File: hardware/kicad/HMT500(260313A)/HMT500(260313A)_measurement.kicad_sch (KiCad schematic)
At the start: 15 parts, among them J3 SM04B-SRSS-TB, U5 PCAP04-AQFM-24, U6 ADS1220IPWR

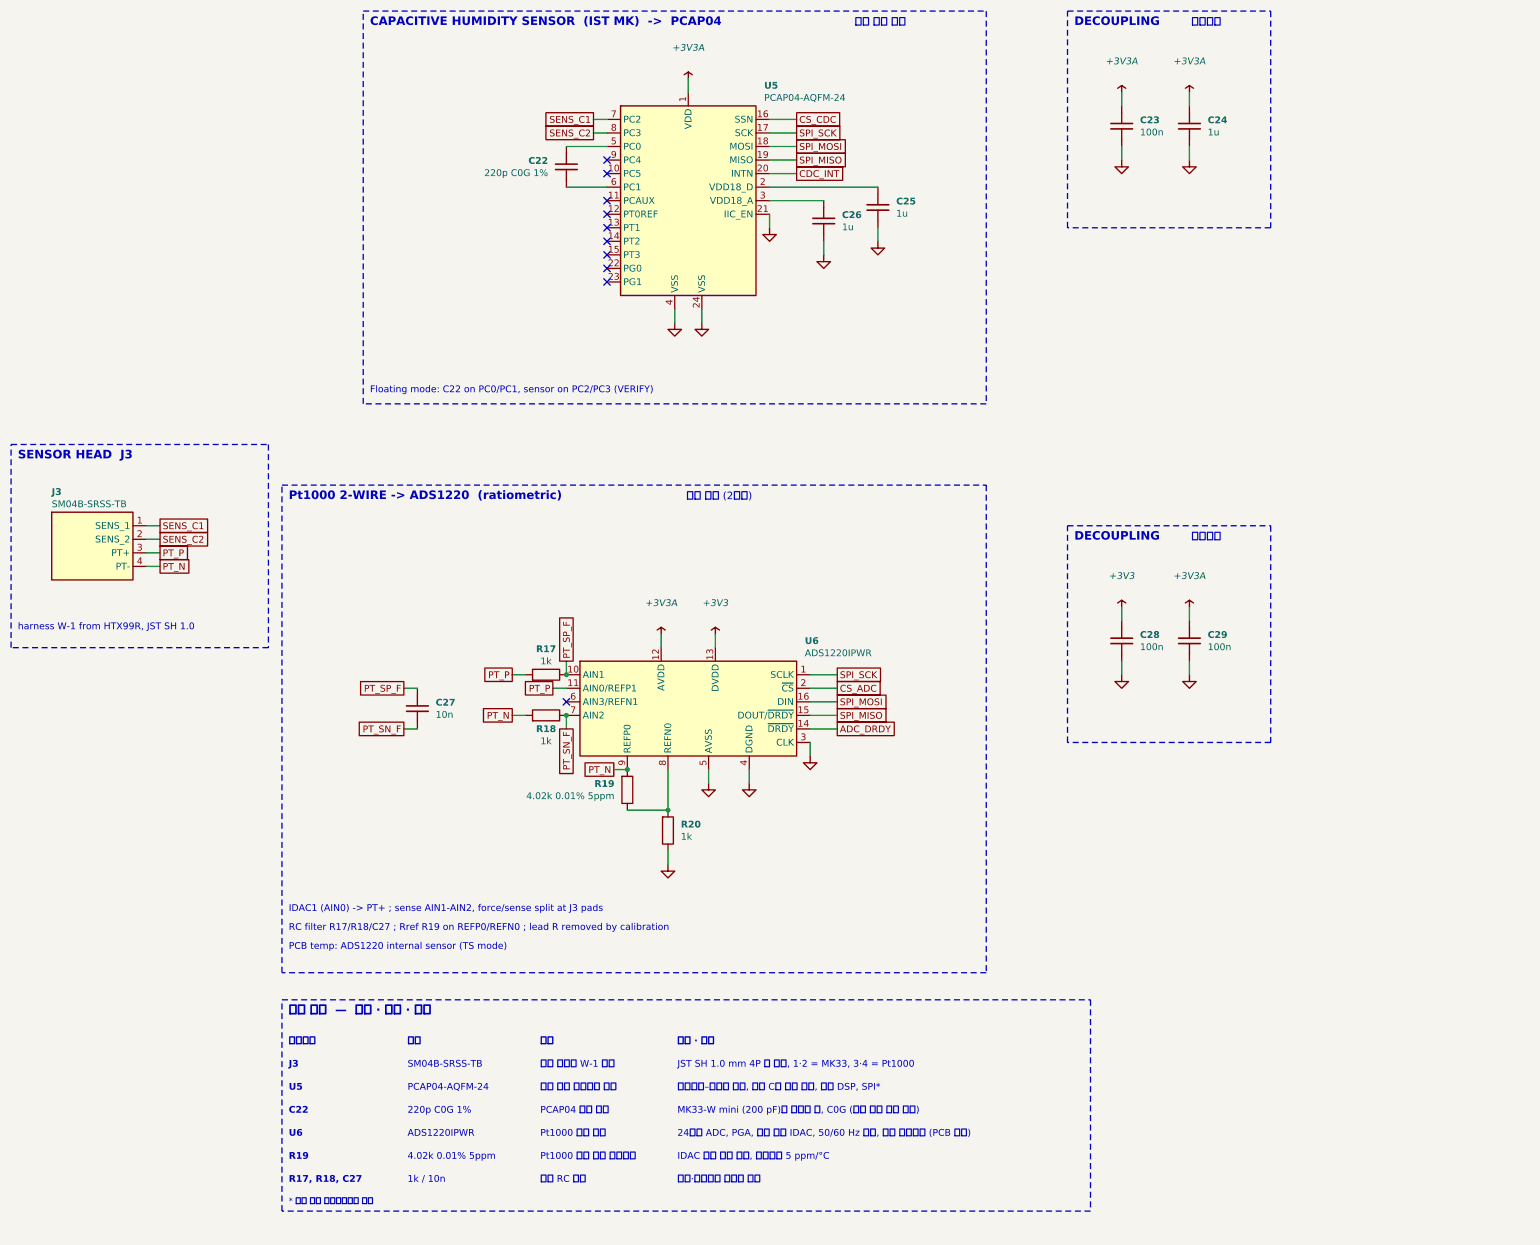
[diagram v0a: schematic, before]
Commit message: Schematic v0.8: apply datasheet review A-O (HMT500(260313A))
- Real pinouts from manufacturer datasheets: LMR36006BRNXR (RNX-12),
  TPS26611DDFR (SOT-23-8), PCAP04 (QFN24); TPS2660 PowerPAD = RTN
- TPS2660: RTN isolated from GND (R22, R7 removed); R5/R6/C4/MODE on
  EF_RTN; R6 80.6k (149 mA); R5 41.2k -> OVP 29 V, supply 12-28 V so
  TPS26611 +Vs stays <= 30 V
- DAC SPI: per-DAC SCLK gating (74LVC2G32, SPI2 mode 3, LATCH1/2 on
  PB10/PB11) - daisy chain was removed in DAC8760 rev D
- DAC AVDD 10R series, ALARM wired-OR with 10k pull-up (PB6)
- Output TVS -> TVS3301 (stacked-pin two-terminal symbol)
- PCAP04 on dedicated SPI3 (PB3/4/5), VDD18 4.7uF, VDD33 10uF
- Buck per datasheet: L 15uH, COUT 2x22uF, CFF 20pF
- Shared VIN_P bulk (C53, C26 removed); PWR_FLT PB7; SGOOD -> PC6/PC7
- Parts list, circuit-design, decision log #26, review doc updated;
  netlist 74/74, 0 errors; tests pass

Co-Authored-By: Claude Opus 5.5 <noreply@anthropic.com>
Claude-Session: https://claude.ai/code/session_01JA2o8uJsqp9Vzsg4b665ev
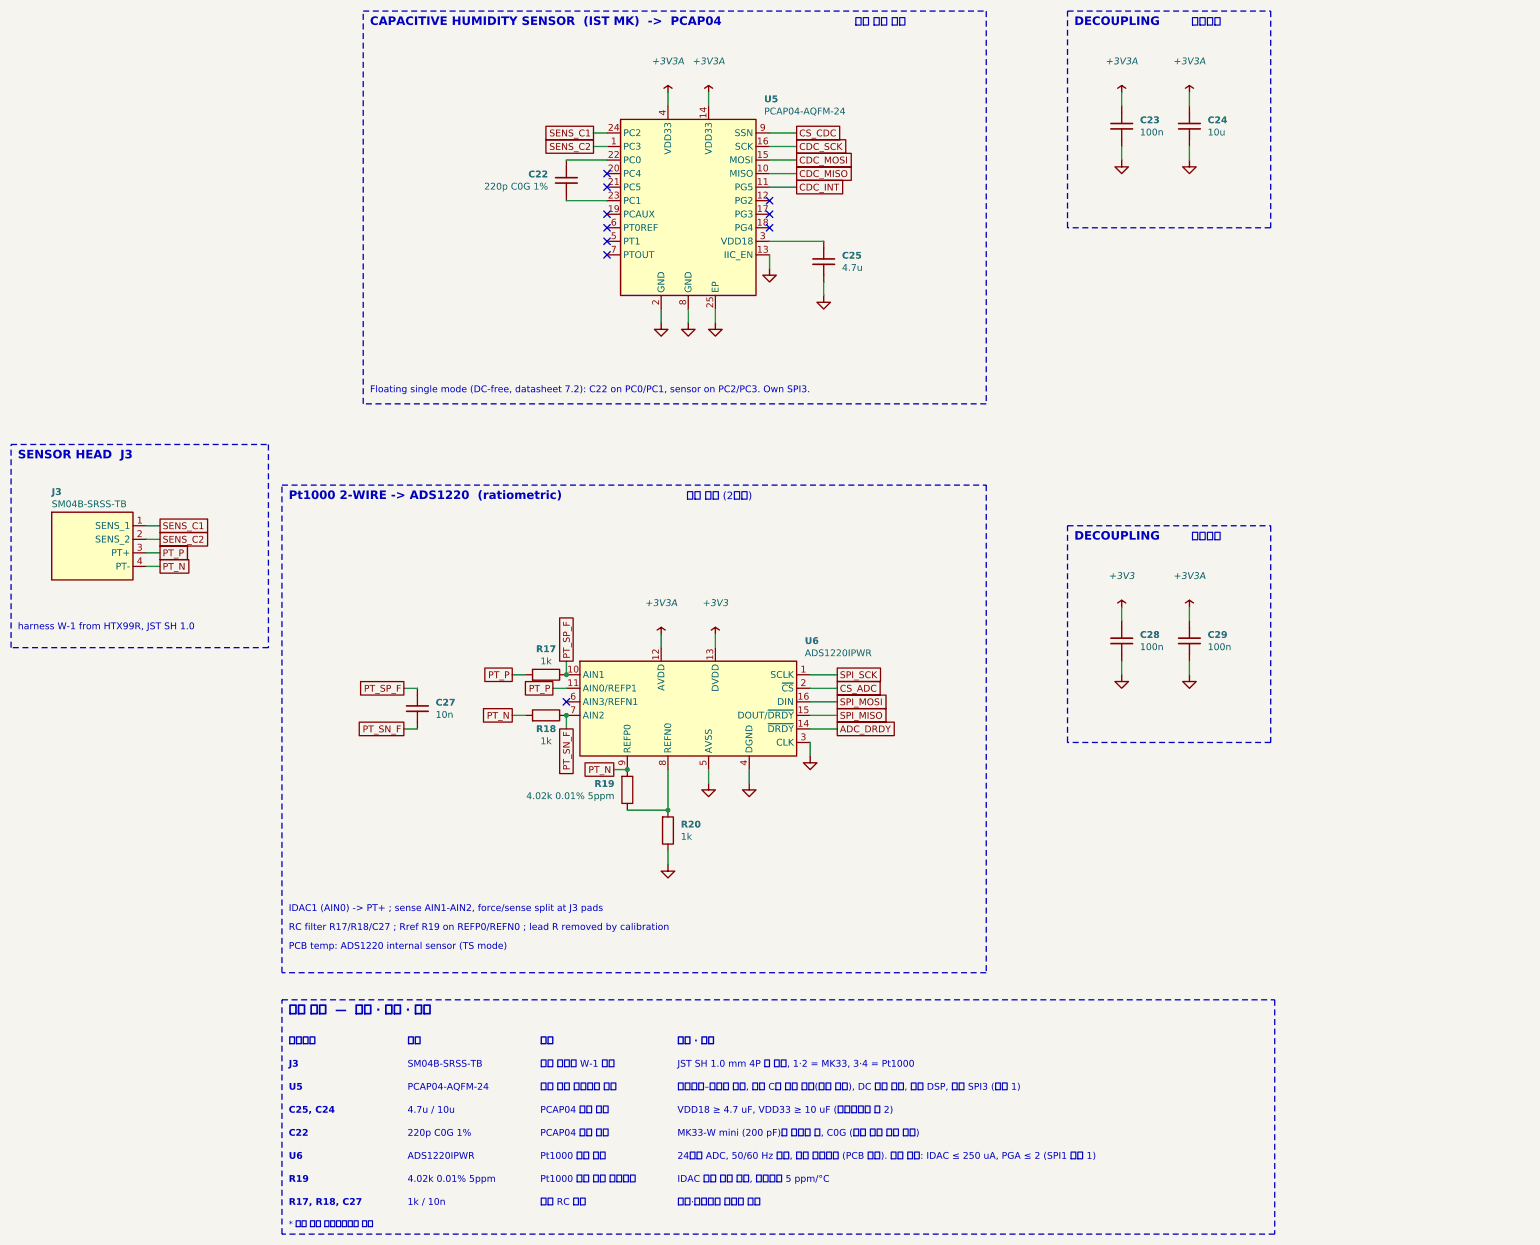
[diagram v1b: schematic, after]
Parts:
- removed C26: 1u, Capacitor_SMD:C_0603_1608Metric, symbol HMT500_260313A:C
- C24: value 1u -> 10u; footprint Capacitor_SMD:C_0603_1608Metric -> Capacitor_SMD:C_0805_2012Metric
- C25: value 1u -> 4.7u; footprint Capacitor_SMD:C_0603_1608Metric -> Capacitor_SMD:C_0805_2012Metric
- U5: footprint TBD:QFN-24_PCAP04 -> Package_DFN_QFN:QFN-24-1EP_4x4mm_P0.5mm_EP2.6x2.6mm; VERIFY YES - pin numbers are placeholders -> (none)
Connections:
- net +3V3A: now also U5.14 (VDD33), U5.4 (VDD33); no longer U5.1 (VDD)
- net CDC_INT: now also U5.11 (PG5); no longer U5.20 (INTN)
- net CS_CDC: now also U5.9 (SSN); no longer U5.16 (SSN)
- net GND: now also U5.13 (IIC_EN), U5.2 (GND), U5.25 (EP), U5.8 (GND); no longer U5.21 (IIC_EN), U5.24 (VSS), U5.4 (VSS)
- net SENS_C1: now also U5.24 (PC2); no longer U5.7 (PC2)
- net SENS_C2: now also U5.1 (PC3); no longer U5.8 (PC3)
- net SPI_MISO: no longer U5.19 (MISO)
- net SPI_MOSI: no longer U5.18 (MOSI)
- net SPI_SCK: no longer U5.17 (SCK)
- net CDC_MISO: now reaches U5.10 (MISO)
- net CDC_MOSI: now reaches U5.15 (MOSI)
- net at C25.1: now also U5.3 (VDD18); no longer U5.2 (VDD18_D)
- net at U5.22 (PC0): now also C22.1
- net at U5.23 (PC1): now also C22.2
- net at U5.5 (PT1): no longer C22.1
- net at U5.6 (PT0REF): no longer C22.2
- new net CDC_SCK: U5.16 (SCK)
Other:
- note added: "24비트 ADC, 50/60 Hz 제거, 내부 온도센서 (PCB 온도). 설정 한계: IDAC ≤ 250 uA, PGA ≤ 2 (SPI1 모드 1)"
- note added: "4.7u / 10u"
- note added: "C25, C24"
- note added: "Floating single mode (DC-free, datasheet 7.2): C22 on PC0/PC1, sensor on PC2/PC3. Own SPI3."
- note added: "PCAP04 전원 버퍼"
- note added: "VDD18 ≥ 4.7 uF, VDD33 ≥ 10 uF (데이터시트 표 2)"
- note added: "정전용량–디지털 변환, 기준 C와 비율 측정(방전 시간), DC 없는 구동, 내부 DSP, 전용 SPI3 (모드 1)"
- note removed: "24비트 ADC, PGA, 여기 전류 IDAC, 50/60 Hz 제거, 내부 온도센서 (PCB 온도)"
- note removed: "Floating mode: C22 on PC0/PC1, sensor on PC2/PC3 (VERIFY)"
- note removed: "정전용량–디지털 변환, 기준 C와 비율 측정, 내부 DSP, SPI*"
- moved on the sheet: C22, C25

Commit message: Schematic: global label shape shows signal direction (driver = output, receiver = input)
Direction derived per net from pin types (output / tri-state / open-drain
drivers, MCU as driver when only inputs are on the other side); analog
and passive nets keep the plain shape, RS-485 bus bidirectional.
Legend line on the root sheet; test for key nets.

Co-Authored-By: Claude Opus 5.5 <noreply@anthropic.com>
Claude-Session: https://claude.ai/code/session_01JA2o8uJsqp9Vzsg4b665ev
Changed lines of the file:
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@@
 (global_label "SENS_C1" (shape passive) (at 124.46 60.96 180) (fields_autoplaced) (effects (font (size 1.27 1.27)) (justify right)) (property "Intersheetrefs" "${INTERSHEET_REFS}" (at 124.46 60.96 0) (effects (font (size 1.27 1.27)) hide)))
 (global_label "SENS_C2" (shape passive) (at 124.46 63.5 180) (fields_autoplaced) (effects (font (size 1.27 1.27)) (justify right)) (property "Intersheetrefs" "${INTERSHEET_REFS}" (at 124.46 63.5 0) (effects (font (size 1.27 1.27)) hide)))
-(global_label "CS_CDC" (shape passive) (at 162.56 60.96 0) (fields_autoplaced) (effects (font (size 1.27 1.27)) (justify left)) (property "Intersheetrefs" "${INTERSHEET_REFS}" (at 162.56 60.96 0) (effects (font (size 1.27 1.27)) hide)))
-(global_label "CDC_SCK" (shape passive) (at 162.56 63.5 0) (fields_autoplaced) (effects (font (size 1.27 1.27)) (justify left)) (property "Intersheetrefs" "${INTERSHEET_REFS}" (at 162.56 63.5 0) (effects (font (size 1.27 1.27)) hide)))
-(global_label "CDC_MOSI" (shape passive) (at 162.56 66.04 0) (fields_autoplaced) (effects (font (size 1.27 1.27)) (justify left)) (property "Intersheetrefs" "${INTERSHEET_REFS}" (at 162.56 66.04 0) (effects (font (size 1.27 1.27)) hide)))
-(global_label "CDC_MISO" (shape passive) (at 162.56 68.58 0) (fields_autoplaced) (effects (font (size 1.27 1.27)) (justify left)) (property "Intersheetrefs" "${INTERSHEET_REFS}" (at 162.56 68.58 0) (effects (font (size 1.27 1.27)) hide)))
-(global_label "CDC_INT" (shape passive) (at 162.56 71.12 0) (fields_autoplaced) (effects (font (size 1.27 1.27)) (justify left)) (property "Intersheetrefs" "${INTERSHEET_REFS}" (at 162.56 71.12 0) (effects (font (size 1.27 1.27)) hide)))
+(global_label "CS_CDC" (shape input) (at 162.56 60.96 0) (fields_autoplaced) (effects (font (size 1.27 1.27)) (justify left)) (property "Intersheetrefs" "${INTERSHEET_REFS}" (at 162.56 60.96 0) (effects (font (size 1.27 1.27)) hide)))
+(global_label "CDC_SCK" (shape input) (at 162.56 63.5 0) (fields_autoplaced) (effects (font (size 1.27 1.27)) (justify left)) (property "Intersheetrefs" "${INTERSHEET_REFS}" (at 162.56 63.5 0) (effects (font (size 1.27 1.27)) hide)))
+(global_label "CDC_MOSI" (shape input) (at 162.56 66.04 0) (fields_autoplaced) (effects (font (size 1.27 1.27)) (justify left)) (property "Intersheetrefs" "${INTERSHEET_REFS}" (at 162.56 66.04 0) (effects (font (size 1.27 1.27)) hide)))
+(global_label "CDC_MISO" (shape output) (at 162.56 68.58 0) (fields_autoplaced) (effects (font (size 1.27 1.27)) (justify left)) (property "Intersheetrefs" "${INTERSHEET_REFS}" (at 162.56 68.58 0) (effects (font (size 1.27 1.27)) hide)))
+(global_label "CDC_INT" (shape output) (at 162.56 71.12 0) (fields_autoplaced) (effects (font (size 1.27 1.27)) (justify left)) (property "Intersheetrefs" "${INTERSHEET_REFS}" (at 162.56 71.12 0) (effects (font (size 1.27 1.27)) hide)))
 (global_label "PT_P" (shape passive) (at 109.22 162.56 180) (fields_autoplaced) (effects (font (size 1.27 1.27)) (justify right)) (property "Intersheetrefs" "${INTERSHEET_REFS}" (at 109.22 162.56 0) (effects (font (size 1.27 1.27)) hide)))
 (global_label "PT_N" (shape passive) (at 109.22 170.18 180) (fields_autoplaced) (effects (font (size 1.27 1.27)) (justify right)) (property "Intersheetrefs" "${INTERSHEET_REFS}" (at 109.22 170.18 0) (effects (font (size 1.27 1.27)) hide)))
@@
 (global_label "PT_SN_F" (shape passive) (at 88.9 172.72 180) (fields_autoplaced) (effects (font (size 1.27 1.27)) (justify right)) (property "Intersheetrefs" "${INTERSHEET_REFS}" (at 88.9 172.72 0) (effects (font (size 1.27 1.27)) hide)))
 (global_label "PT_N" (shape passive) (at 128.27 180.34 180) (fields_autoplaced) (effects (font (size 1.27 1.27)) (justify right)) (property "Intersheetrefs" "${INTERSHEET_REFS}" (at 128.27 180.34 0) (effects (font (size 1.27 1.27)) hide)))
-(global_label "SPI_SCK" (shape passive) (at 170.18 162.56 0) (fields_autoplaced) (effects (font (size 1.27 1.27)) (justify left)) (property "Intersheetrefs" "${INTERSHEET_REFS}" (at 170.18 162.56 0) (effects (font (size 1.27 1.27)) hide)))
-(global_label "CS_ADC" (shape passive) (at 170.18 165.1 0) (fields_autoplaced) (effects (font (size 1.27 1.27)) (justify left)) (property "Intersheetrefs" "${INTERSHEET_REFS}" (at 170.18 165.1 0) (effects (font (size 1.27 1.27)) hide)))
-(global_label "SPI_MOSI" (shape passive) (at 170.18 167.64 0) (fields_autoplaced) (effects (font (size 1.27 1.27)) (justify left)) (property "Intersheetrefs" "${INTERSHEET_REFS}" (at 170.18 167.64 0) (effects (font (size 1.27 1.27)) hide)))
-(global_label "SPI_MISO" (shape passive) (at 170.18 170.18 0) (fields_autoplaced) (effects (font (size 1.27 1.27)) (justify left)) (property "Intersheetrefs" "${INTERSHEET_REFS}" (at 170.18 170.18 0) (effects (font (size 1.27 1.27)) hide)))
-(global_label "ADC_DRDY" (shape passive) (at 170.18 172.72 0) (fields_autoplaced) (effects (font (size 1.27 1.27)) (justify left)) (property "Intersheetrefs" "${INTERSHEET_REFS}" (at 170.18 172.72 0) (effects (font (size 1.27 1.27)) hide)))
+(global_label "SPI_SCK" (shape input) (at 170.18 162.56 0) (fields_autoplaced) (effects (font (size 1.27 1.27)) (justify left)) (property "Intersheetrefs" "${INTERSHEET_REFS}" (at 170.18 162.56 0) (effects (font (size 1.27 1.27)) hide)))
+(global_label "CS_ADC" (shape input) (at 170.18 165.1 0) (fields_autoplaced) (effects (font (size 1.27 1.27)) (justify left)) (property "Intersheetrefs" "${INTERSHEET_REFS}" (at 170.18 165.1 0) (effects (font (size 1.27 1.27)) hide)))
+(global_label "SPI_MOSI" (shape input) (at 170.18 167.64 0) (fields_autoplaced) (effects (font (size 1.27 1.27)) (justify left)) (property "Intersheetrefs" "${INTERSHEET_REFS}" (at 170.18 167.64 0) (effects (font (size 1.27 1.27)) hide)))
+(global_label "SPI_MISO" (shape output) (at 170.18 170.18 0) (fields_autoplaced) (effects (font (size 1.27 1.27)) (justify left)) (property "Intersheetrefs" "${INTERSHEET_REFS}" (at 170.18 170.18 0) (effects (font (size 1.27 1.27)) hide)))
+(global_label "ADC_DRDY" (shape output) (at 170.18 172.72 0) (fields_autoplaced) (effects (font (size 1.27 1.27)) (justify left)) (property "Intersheetrefs" "${INTERSHEET_REFS}" (at 170.18 172.72 0) (effects (font (size 1.27 1.27)) hide)))
 (no_connect (at 127 68.58))
 (no_connect (at 127 71.12))

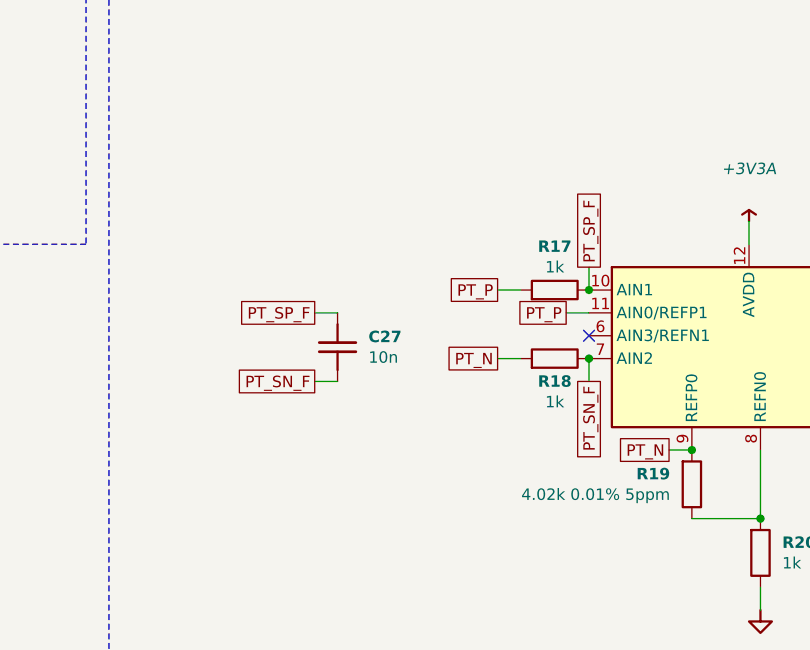
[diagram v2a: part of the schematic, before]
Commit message: Schematic: wire nearby same-sheet nets, signal-flow direction for analog nets
- Analog: +VSENSE and terminal feedback drawn as wires to the OPA197
  buffer (no DACn_SENSE / second OUTn_EXT labels); U14 1A/2A tied, one
  DAC_SCK label
- Power: TPS2660 left pins reordered so R3-R5 run straight from IN to
  UVLO/OVP; one VIN_F label
- Measurement: C27 sits directly between R17/R18 and AIN1/AIN2
- MCU: SWD pads (J2) placed on the PA13/PA14 rows and wired directly
- Label direction for passive nets from signal flow: OUTn_EXT analog ->
  connector, VIN_F connector -> eFuse, BUCK_FB divider -> FB
- Tests: nearby same-sheet labels must be wired; bend limit 6/sheet;
  check_netlist accepts KiCad auto-named multi-pin nets

Co-Authored-By: Claude Opus 5.5 <noreply@anthropic.com>
Claude-Session: https://claude.ai/code/session_01JA2o8uJsqp9Vzsg4b665ev
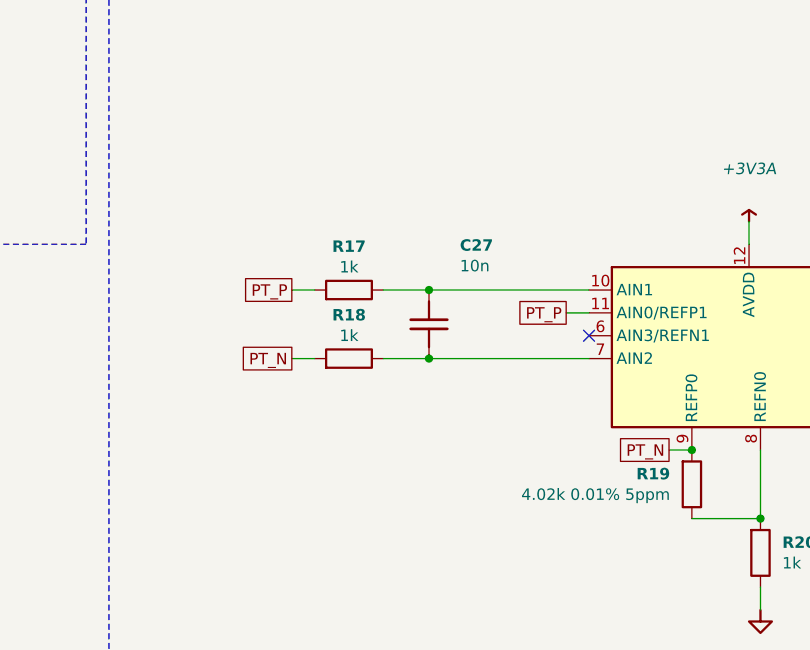
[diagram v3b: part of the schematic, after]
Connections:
- net PT_SN_F: no longer names the net of C27.2, R18.2, U6.7 (AIN2)
- net PT_SP_F: no longer names the net of C27.1, R17.2, U6.10 (AIN1)
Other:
- moved on the sheet: C27, R17, R18
